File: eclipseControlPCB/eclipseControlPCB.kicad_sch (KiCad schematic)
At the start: 51 parts, among them J1 LINE_RF, J10 LINE_RB, J11 LINE_LB, J12 DIST_CL, J14 Conn_01x02_Pin, J15 DIST_CR, J16 Conn_02x05_Odd_Even, J2 DIST_L, J3 DIST_R, J4 DIST_C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

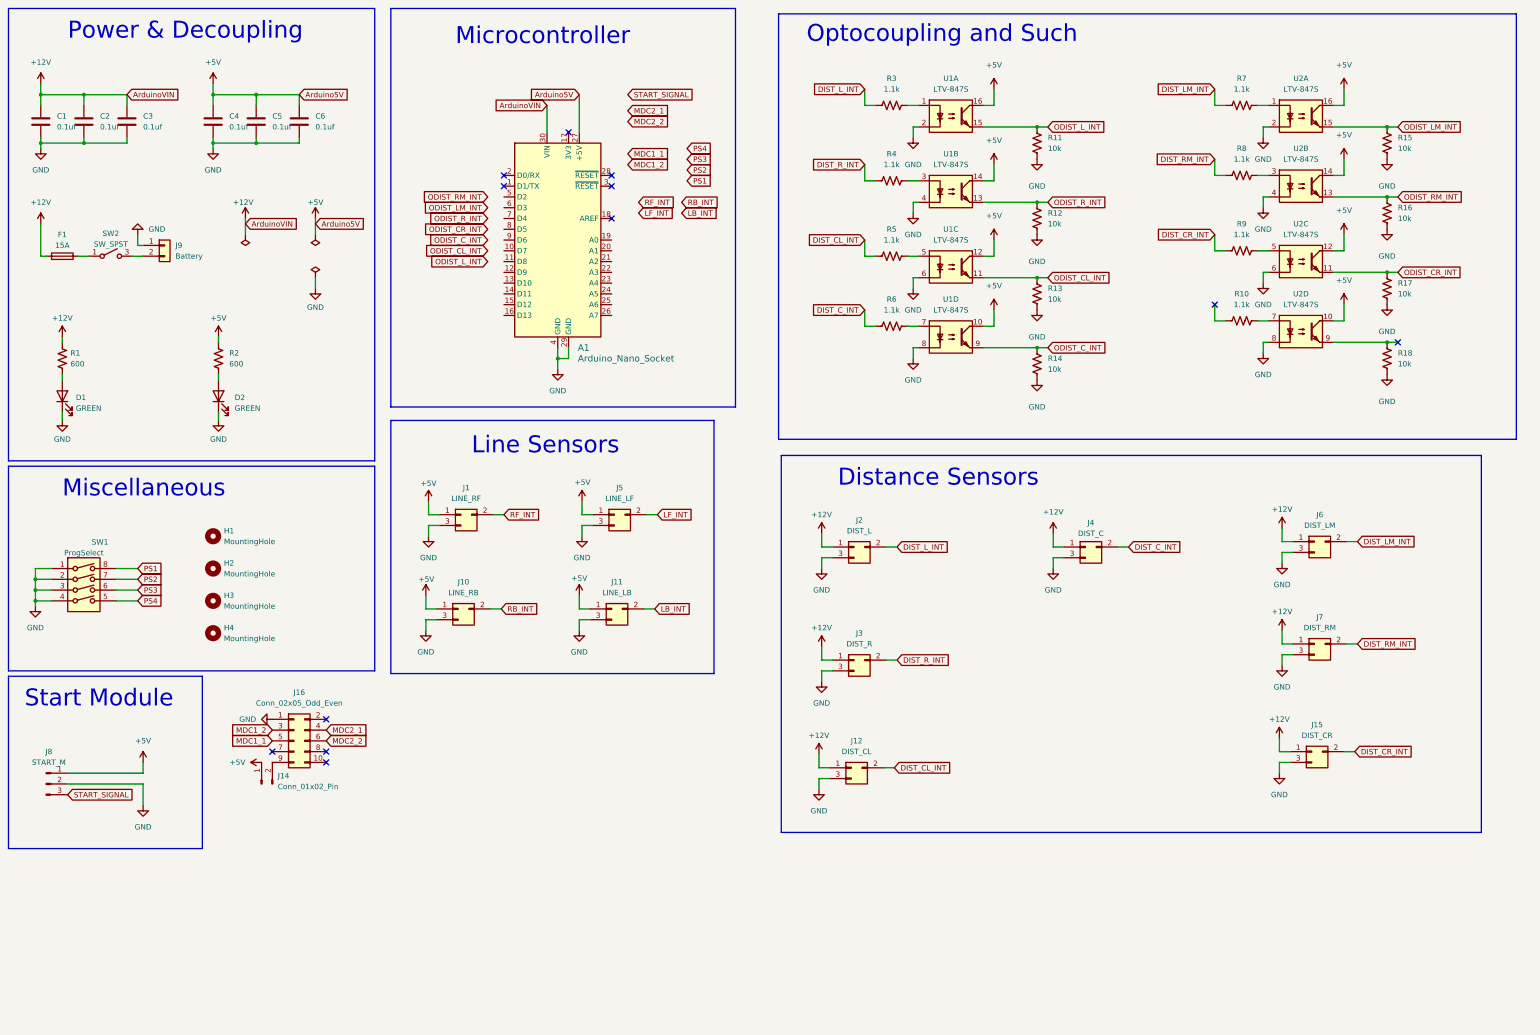
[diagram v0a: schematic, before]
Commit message: no optocoupler implementation
board layout designed to stack on aliexpress motor driver
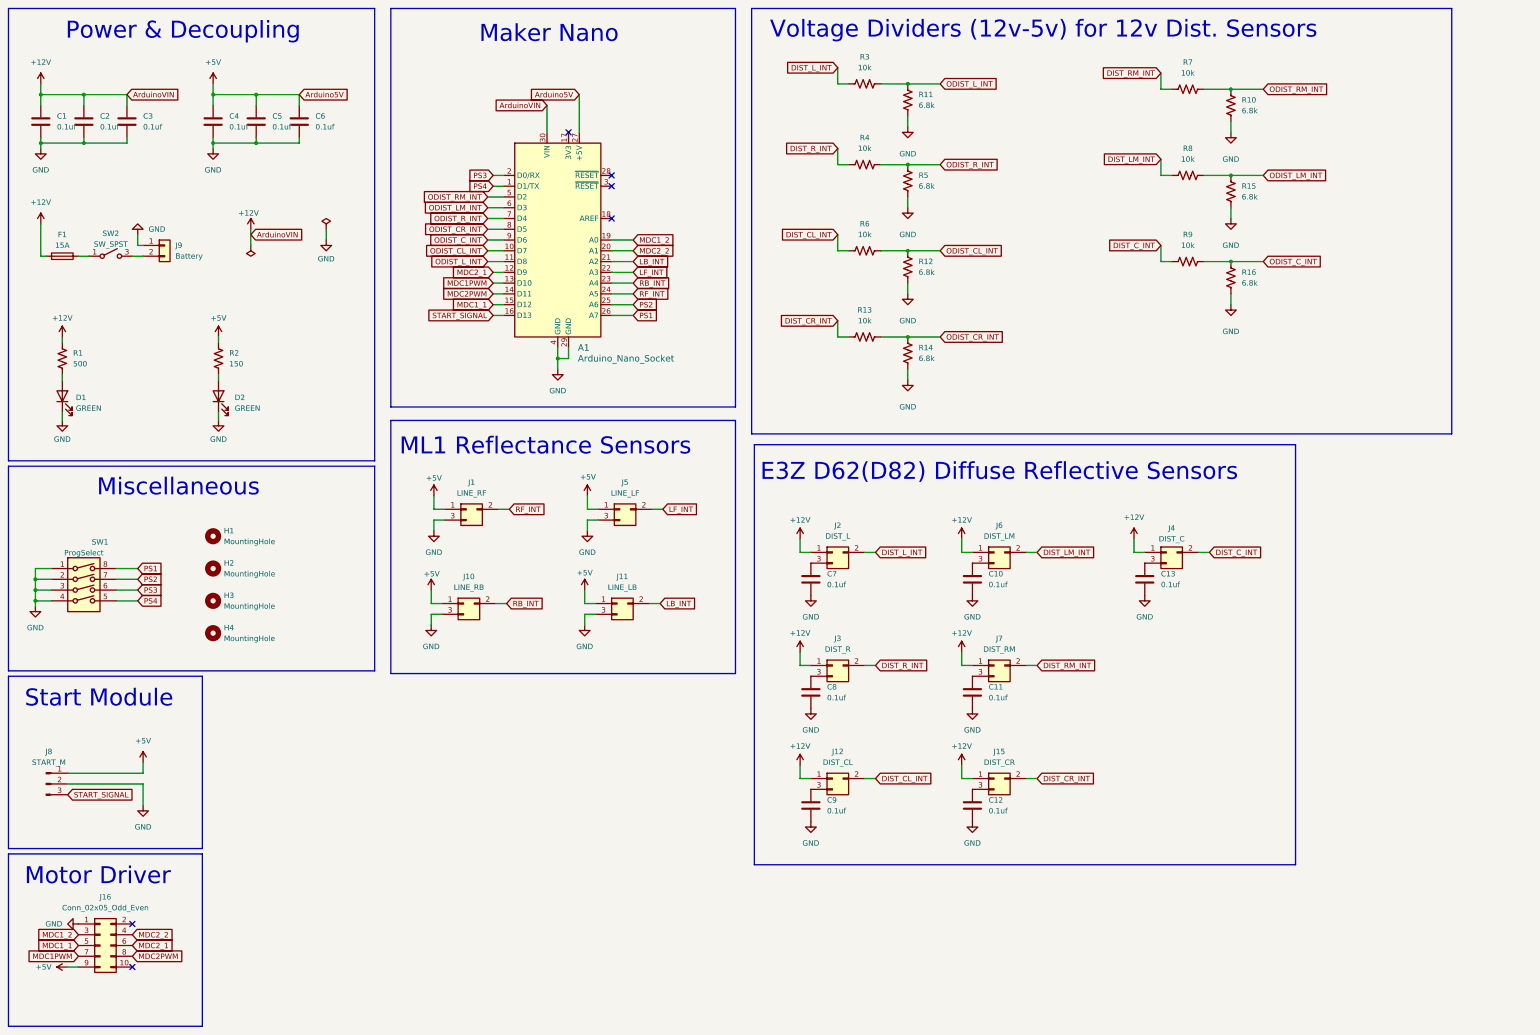
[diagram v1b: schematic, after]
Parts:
- removed J14: Conn_01x02_Pin, Connector_PinHeader_2.54mm:PinHeader_1x02_P2.54mm_Vertical, symbol Connector:Conn_01x02_Pin
- removed R17, R18: 10k, symbol Device:R_US
- removed U1, U2: LTV-847S, Package_DIP:SMDIP-16_W9.53mm, symbol Isolator:LTV-847S
- added C10, C11, C12, C13, C7, C8, C9: 0.1uf, Capacitor_SMD:C_0805_2012Metric_Pad1.18x1.45mm_HandSolder, symbol Device:C
- J9: footprint Connector_AMASS:AMASS_XT30U-M_1x02_P5.0mm_Vertical -> TerminalBlock:TerminalBlock_Altech_AK300-2_P5.00mm
- R1: value 600 -> 500
- R10, R5: value 1.1k -> 6.8k; footprint (none) -> Resistor_SMD:R_0805_2012Metric_Pad1.20x1.40mm_HandSolder
- R11, R12, R14, R15, R16: value 10k -> 6.8k; footprint (none) -> Resistor_SMD:R_0805_2012Metric_Pad1.20x1.40mm_HandSolder
- R13: footprint (none) -> Resistor_SMD:R_0805_2012Metric_Pad1.20x1.40mm_HandSolder
- R2: value 600 -> 150
- R3, R4, R6, R7, R8, R9: value 1.1k -> 10k; footprint (none) -> Resistor_SMD:R_0805_2012Metric_Pad1.20x1.40mm_HandSolder
- SW1: footprint Button_Switch_SMD:SW_DIP_SPSTx03_Slide_9.78x9.8mm_W8.61mm_P2.54mm -> Button_Switch_SMD:SW_DIP_SPSTx04_Slide_6.7x11.72mm_W6.73mm_P2.54mm_LowProfile_JPin
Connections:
- net +5V: now also J16.9 (Pin_9)
- net DIST_CL_INT: now also R6.1; no longer R5.1
- net DIST_CR_INT: now also R13.1; no longer R9.1
- net DIST_C_INT: now also R9.1; no longer R6.1
- net DIST_LM_INT: now also R8.1; no longer R7.1
- net DIST_RM_INT: now also R7.1; no longer R8.1
- net GND: now also R10.1, R5.1, C10.2, C11.2, C12.2, C13.2, C7.2, C8.2, C9.2; no longer J12.3 (Pin_3), J15.3 (Pin_3), J2.3 (Pin_3), J3.3 (Pin_3), J4.3 (Pin_3), J6.3 (Pin_3), J7.3 (Pin_3), R13.1
- net LB_INT: now also A1.21 (A2)
- net LF_INT: now also A1.22 (A3)
- net MDC1_1: now also A1.15 (D12)
- net MDC1_2: now also A1.19 (A0)
- net MDC2_1: now also A1.12 (D9), J16.6 (Pin_6); no longer J16.4 (Pin_4)
- net MDC2_2: now also A1.20 (A1), J16.4 (Pin_4); no longer J16.6 (Pin_6)
- net ODIST_CL_INT: now also A1.10 (D7), R12.2, R6.2; no longer R13.2
- net ODIST_CR_INT: now also A1.8 (D5), R13.2, R14.2
- net ODIST_C_INT: now also A1.9 (D6), R16.2, R9.2; no longer R14.2
- net ODIST_LM_INT: now also A1.6 (D3), R8.2
- net ODIST_L_INT: now also A1.11 (D8), R3.2
- net ODIST_RM_INT: now also A1.5 (D2), R10.2, R7.2; no longer R16.2
- net ODIST_R_INT: now also A1.7 (D4), R4.2, R5.2; no longer R12.2
- net PS1: now also A1.26 (A7)
- net PS2: now also A1.25 (A6)
- net PS3: now also A1.2 (D0/RX)
- net PS4: now also A1.1 (D1/TX)
- net RB_INT: now also A1.23 (A4)
- net RF_INT: now also A1.24 (A5)
- net START_SIGNAL: now also A1.16 (D13)
- net MDC1PWM: now reaches A1.13 (D10)
- net MDC1PWM: now also J16.7 (Pin_7)
- net MDC2PWM: now reaches A1.14 (D11)
- net MDC2PWM: now also J16.8 (Pin_8)
- new net: C12.1, J15.3 (Pin_3)
- new net: C10.1, J6.3 (Pin_3)
- new net: C9.1, J12.3 (Pin_3)
- new net: C7.1, J2.3 (Pin_3)
- new net: C11.1, J7.3 (Pin_3)
- new net: C8.1, J3.3 (Pin_3)
- new net: C13.1, J4.3 (Pin_3)
- no-connect marks 12 -> 6
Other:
- note added: "E3Z D62(D82) Diffuse Reflective Sensors"
- note added: "ML1 Reflectance Sensors"
- note added: "Maker Nano"
- note added: "Motor Driver"
- note added: "Voltage Dividers (12v-5v) for 12v Dist. Sensors"
- note removed: "Distance Sensors"
- note removed: "Line Sensors"
- note removed: "Microcontroller"
- note removed: "Optocoupling and Such"
- moved on the sheet: J1, J10, J11, J12, J15, J16, J2, J3, J4, J5, J6, J7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
